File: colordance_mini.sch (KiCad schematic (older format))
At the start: 36 parts, among them J1 CONN_02X08, J2 CONN_02X08, SW1 Rotary_Encoder, SW2 Rotary_Encoder, SW3 Rotary_Encoder, SW4 Rotary_Encoder

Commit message: Create the PCB. This is rev v1.0, I requested 5 boards from EasyEDA. As-yet untested.
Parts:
- removed J2: CONN_02X08, symbol CONN_02X08
- added C10: 10uF, Capacitors_THT:CP_Radial_D5.0mm_P2.00mm, symbol CP
- added C9: .01uF, Capacitors_THT:C_Disc_D5.0mm_W2.5mm_P5.00mm, symbol C
- C1, C2, C3, C4, C5, C6, C7, C8: footprint (none) -> Capacitors_THT:C_Disc_D5.0mm_W2.5mm_P5.00mm
- J1: footprint (none) -> Pin_Headers:Pin_Header_Straight_2x08_Pitch2.54mm
- R1, R10, R11, R12, R13, R14, R15, R16, R2, R3, R4, R5, R6, R7, R8, R9: footprint (none) -> Resistors_THT:R_Axial_DIN0207_L6.3mm_D2.5mm_P7.62mm_Horizontal
- RV1, RV2, RV3, RV4, RV5, RV6: footprint (none) -> homebrew:BOURNS_SLIDE_POT
- SW1, SW2, SW3, SW4: footprint (none) -> homebrew:BOURNS_PEC11R_ENCODER
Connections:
- net labels added: SAT, VAL
- net labels removed: SATURATION, VALUE
- wire segments 112 -> 98
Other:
- moved on the sheet: RV2, RV3, RV4, RV5, RV6

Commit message: Add front panel SVG v1.0
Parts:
- RV1, RV2, RV3, RV4, RV5, RV6: footprint homebrew:BOURNS_SLIDE_POT -> homebrew:BOURNS_SLIDE_POT_45MM
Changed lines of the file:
@@
 LIBS:contrib
 LIBS:valves
+LIBS:colordance_mini-cache
 EELAYER 25 0
 EELAYER END
@@
 F 0 "RV1" V 625 2300 50  0000 C CNN
 F 1 "POT" V 700 2300 50  0000 C CNN
-F 2 "homebrew:BOURNS_SLIDE_POT" H 800 2300 50  0001 C CNN
+F 2 "homebrew:BOURNS_SLIDE_POT_45MM" H 800 2300 50  0001 C CNN
 F 3 "" H 800 2300 50  0001 C CNN
 	1    800  2300
@@
 F 0 "RV2" V 1325 2300 50  0000 C CNN
 F 1 "POT" V 1400 2300 50  0000 C CNN
-F 2 "homebrew:BOURNS_SLIDE_POT" H 1500 2300 50  0001 C CNN
+F 2 "homebrew:BOURNS_SLIDE_POT_45MM" H 1500 2300 50  0001 C CNN
 F 3 "" H 1500 2300 50  0001 C CNN
 	1    1500 2300
@@
 F 0 "RV3" V 2025 2300 50  0000 C CNN
 F 1 "POT" V 2100 2300 50  0000 C CNN
-F 2 "homebrew:BOURNS_SLIDE_POT" H 2200 2300 50  0001 C CNN
+F 2 "homebrew:BOURNS_SLIDE_POT_45MM" H 2200 2300 50  0001 C CNN
 F 3 "" H 2200 2300 50  0001 C CNN
 	1    2200 2300
@@
 F 0 "RV4" V 2875 2300 50  0000 C CNN
 F 1 "POT" V 2950 2300 50  0000 C CNN
-F 2 "homebrew:BOURNS_SLIDE_POT" H 3050 2300 50  0001 C CNN
+F 2 "homebrew:BOURNS_SLIDE_POT_45MM" H 3050 2300 50  0001 C CNN
 F 3 "" H 3050 2300 50  0001 C CNN
 	1    3050 2300
@@
 F 0 "RV5" V 3575 2300 50  0000 C CNN
 F 1 "POT" V 3650 2300 50  0000 C CNN
-F 2 "homebrew:BOURNS_SLIDE_POT" H 3750 2300 50  0001 C CNN
+F 2 "homebrew:BOURNS_SLIDE_POT_45MM" H 3750 2300 50  0001 C CNN
 F 3 "" H 3750 2300 50  0001 C CNN
 	1    3750 2300
@@
 F 0 "RV6" V 4375 2300 50  0000 C CNN
 F 1 "POT" V 4450 2300 50  0000 C CNN
-F 2 "homebrew:BOURNS_SLIDE_POT" H 4550 2300 50  0001 C CNN
+F 2 "homebrew:BOURNS_SLIDE_POT_45MM" H 4550 2300 50  0001 C CNN
 F 3 "" H 4550 2300 50  0001 C CNN
 	1    4550 2300

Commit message: Add a teensy and a whole bunch of actuators for v1.1.
Layout not yet updated.
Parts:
- removed C10: 10uF, Capacitors_THT:CP_Radial_D5.0mm_P2.00mm, symbol CP
- removed J1: CONN_02X08, Pin_Headers:Pin_Header_Straight_2x08_Pitch2.54mm, symbol CONN_02X08
- added C12, C8: 10uF, Capacitors_THT:C_Disc_D5.0mm_W2.5mm_P5.00mm, symbol C
- added C7: .01uF, Capacitors_THT:C_Disc_D5.0mm_W2.5mm_P5.00mm, symbol C
- added J1: XLR3, symbol XLR3
- added J10: CONN_01X06, symbol CONN_01X06
- added J11, J12, J17, J3, J5, J7, J8, J9: CONN_01X04, symbol CONN_01X04
- added J13, J14, J15, J16, J4, J6: CONN_01X03, symbol CONN_01X03
- added J2: CONN_01X08, symbol CONN_01X08
- added R1: 120, symbol R
- added R2: 3k3, symbol R
- added R22: 470, symbol R
- added R23, R24, R25: 4k7, symbol R
- added R3: 1k, symbol R
- added R4, R5: 562, symbol R
- added U1: MAX485CSA+, 21-0041B_8, symbol MAX485CSA+
- added U2: ROE-0505S, symbol ROE-0505S
- added U3: 6N137, DIP762W50P254L977H451Q8, symbol 6N137
- added U4: Teensy3.5, symbol Teensy3.5-RESCUE-colordance_mini
- renumbered C8 to C10, C9 to C11, C7 to C9, R5 to R10, R6 to R11, R7 to R12, R8 to R13, R9 to R14, R10 to R15, R11 to R16, R12 to R17, R13 to R18, R14 to R19, R15 to R20, R16 to R21, R1 to R6, R2 to R7, R3 to R8, R4 to R9, RV3 to RV2, RV4 to RV3, RV5 to RV4, RV6 to RV5, RV2 to RV6
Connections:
- net labels added: +3V3, +5V, +BATT, AUX_CS, AUX_MISO, AUX_MOSI, AUX_PIN_1, AUX_PIN_2, AUX_RX, AUX_SCK, AUX_TX, DENSITY, DMX_3V3, DMX_3V3_ISO, HUE_0_A, HUE_0_B, HUE_1_A, HUE_1_B, HUE_2_A, HUE_2_B, MIC_IN, MOTION_1, MOTION_2, MOTION_3, MOTION_4, NEXT_EFFECT, NEXT_EFFECT_LED, ON_BUTTON, ON_BUTTON_LED, ORIENTATION, ORIENTATION_LED, PARAM, PREV_EFFECT, PREV_EFFECT_LED, SCL0, SDA0, SERIAL_LOG_OUT, SPI_LED_MOSI, SPI_LED_SCK, TEMPO_A, TEMPO_B, TEMPO_TAP, TEMPO_TAP_LED, VBATT_DIV, VDMX
- net labels removed: E1_A, E1_B, E2_A, E2_B, E3_A, E3_B, HUE_A, HUE_B, SAT, VAL, VCC
- wire segments 98 -> 101
- no-connect marks 0 -> 37
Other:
- note added: "Aux connections"
- note added: "Aux pins"
- note added: "Battery voltage monitor"
- note added: "Buttons"
- note added: "DMX"
- note added: "DMX power isolation"
- note added: "DMX signal isolation"
- note added: "External mic"
- note added: "I2C"
- note added: "Logger"
- note added: "Motion sensors"
- note added: "On button"
- note added: "Orientation"
- note added: "Power"
- note added: "Prev/next effect"
- note added: "SPI"
- note added: "SPI LED connections"
- note added: "Serial"
- note added: "Tempo"
- moved on the sheet: C11, RV2, RV3, RV4, RV5, RV6

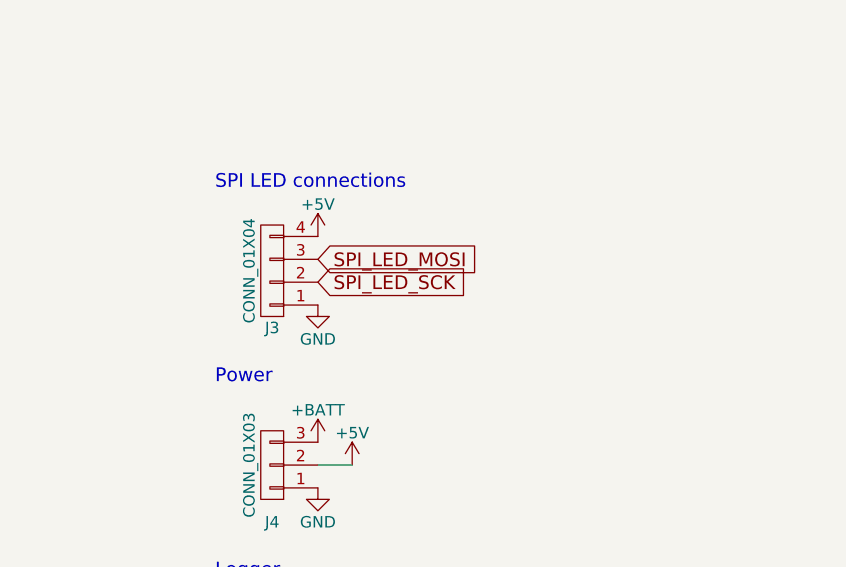
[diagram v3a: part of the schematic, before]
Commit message: Add an onboard APA102 LED
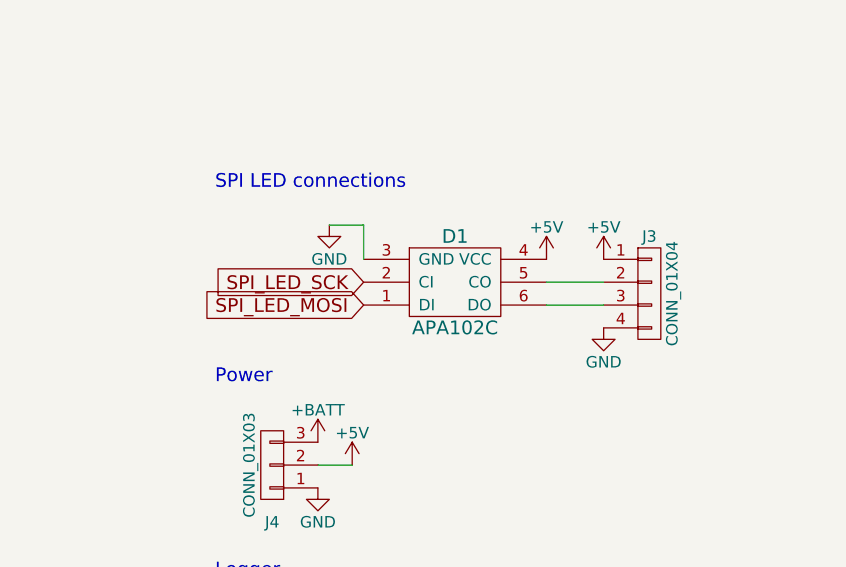
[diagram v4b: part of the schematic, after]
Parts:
- added D1: APA102C, symbol APA102C
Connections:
- net +5V: now also J3.1 (P1), D1.4 (VCC); no longer J3.4 (P4)
- net GND: now also J3.4 (P4), D1.3 (GND); no longer J3.1 (P1)
- net SPI_LED_MOSI: now also D1.1 (DI); no longer J3.3 (P3)
- net SPI_LED_SCK: now also D1.2 (CI); no longer J3.2 (P2)
- new net: D1.5 (CO), J3.2 (P2)
- new net: D1.6 (DO), J3.3 (P3)
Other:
- moved on the sheet: J3
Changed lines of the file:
@@
 L CONN_01X04 J3
 U 1 1 5ABFCD70
-P 12250 5550
-F 0 "J3" H 12250 5800 50  0000 C CNN
-F 1 "CONN_01X04" V 12350 5550 50  0000 C CNN
-F 2 "" H 12250 5550 50  0001 C CNN
-F 3 "" H 12250 5550 50  0001 C CNN
-	1    12250 5550
-	-1   0    0    1
+P 13900 5650
+F 0 "J3" H 13900 5900 50  0000 C CNN
+F 1 "CONN_01X04" V 14000 5650 50  0000 C CNN
+F 2 "" H 13900 5650 50  0001 C CNN
+F 3 "" H 13900 5650 50  0001 C CNN
+	1    13900 5650
+	1    0    0    -1
 $EndComp
 Text Notes 12000 5200 0    60   ~ 0
 SPI LED connections
-Text GLabel 12450 5500 2    60   Input ~ 0
+Text GLabel 12650 5700 0    60   Input ~ 0
 SPI_LED_MOSI
-Text GLabel 12450 5600 2    60   Input ~ 0
+Text GLabel 12650 5600 0    60   Input ~ 0
 SPI_LED_SCK
 $Comp
 L +5V #PWR039
 U 1 1 5ABFD543
-P 12450 5400
-F 0 "#PWR039" H 12450 5250 50  0001 C CNN
-F 1 "+5V" H 12450 5540 50  0000 C CNN
-F 2 "" H 12450 5400 50  0001 C CNN
-F 3 "" H 12450 5400 50  0001 C CNN
-	1    12450 5400
+P 13700 5500
+F 0 "#PWR039" H 13700 5350 50  0001 C CNN
+F 1 "+5V" H 13700 5640 50  0000 C CNN
+F 2 "" H 13700 5500 50  0001 C CNN
+F 3 "" H 13700 5500 50  0001 C CNN
+	1    13700 5500
 	1    0    0    -1
 $EndComp
@@
 L GND #PWR040
 U 1 1 5ABFD6A5
-P 12450 5700
-F 0 "#PWR040" H 12450 5450 50  0001 C CNN
-F 1 "GND" H 12450 5550 50  0000 C CNN
-F 2 "" H 12450 5700 50  0001 C CNN
-F 3 "" H 12450 5700 50  0001 C CNN
-	1    12450 5700
+P 13700 5800
+F 0 "#PWR040" H 13700 5550 50  0001 C CNN
+F 1 "GND" H 13700 5650 50  0000 C CNN
+F 2 "" H 13700 5800 50  0001 C CNN
+F 3 "" H 13700 5800 50  0001 C CNN
+	1    13700 5800
 	1    0    0    -1
 $EndComp
@@
 NoConn ~ 19050 4000
 Connection ~ 1250 9150
+$Comp
+L APA102C D1
+U 1 1 5AC13E31
+P 13050 5600
+F 0 "D1" H 13050 5800 60  0000 C CNN
+F 1 "APA102C" H 13050 5400 60  0000 C CNN
+F 2 "" H 13050 5600 60  0001 C CNN
+F 3 "" H 13050 5600 60  0001 C CNN
+	1    13050 5600
+	1    0    0    -1
+$EndComp
+$Comp
+L GND #PWR072
+U 1 1 5AC140CF
+P 12500 5350
+F 0 "#PWR072" H 12500 5100 50  0001 C CNN
+F 1 "GND" H 12500 5200 50  0000 C CNN
+F 2 "" H 12500 5350 50  0001 C CNN
+F 3 "" H 12500 5350 50  0001 C CNN
+	1    12500 5350
+	1    0    0    -1
+$EndComp
+Wire Wire Line
+	12500 5350 12650 5350
+Wire Wire Line
+	12650 5350 12650 5500
+$Comp
+L +5V #PWR073
+U 1 1 5AC14273
+P 13450 5500
+F 0 "#PWR073" H 13450 5350 50  0001 C CNN
+F 1 "+5V" H 13450 5640 50  0000 C CNN
+F 2 "" H 13450 5500 50  0001 C CNN
+F 3 "" H 13450 5500 50  0001 C CNN
+	1    13450 5500
+	1    0    0    -1
+$EndComp
+Wire Wire Line
+	13450 5600 13700 5600
+Wire Wire Line
+	13700 5700 13450 5700
 $EndSCHEMATC

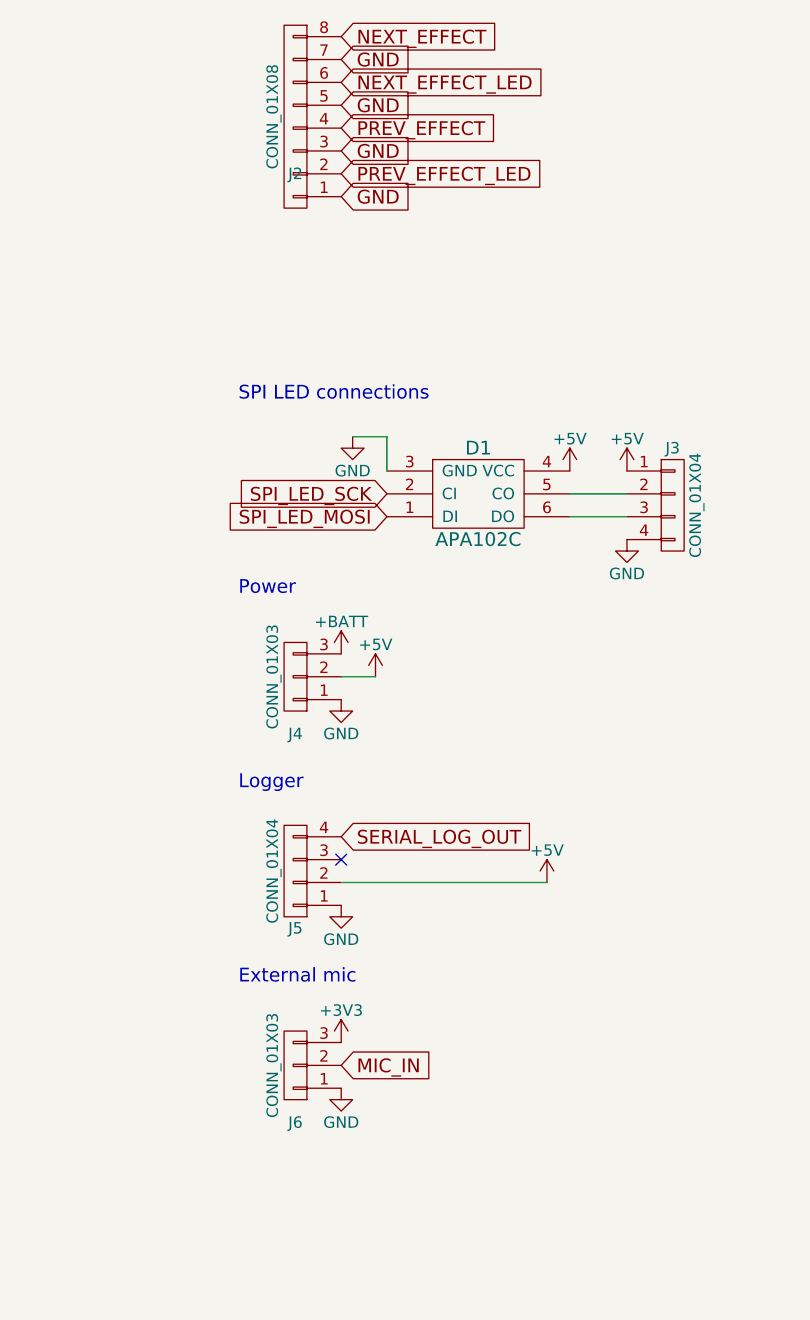
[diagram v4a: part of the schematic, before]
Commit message: Rough placement
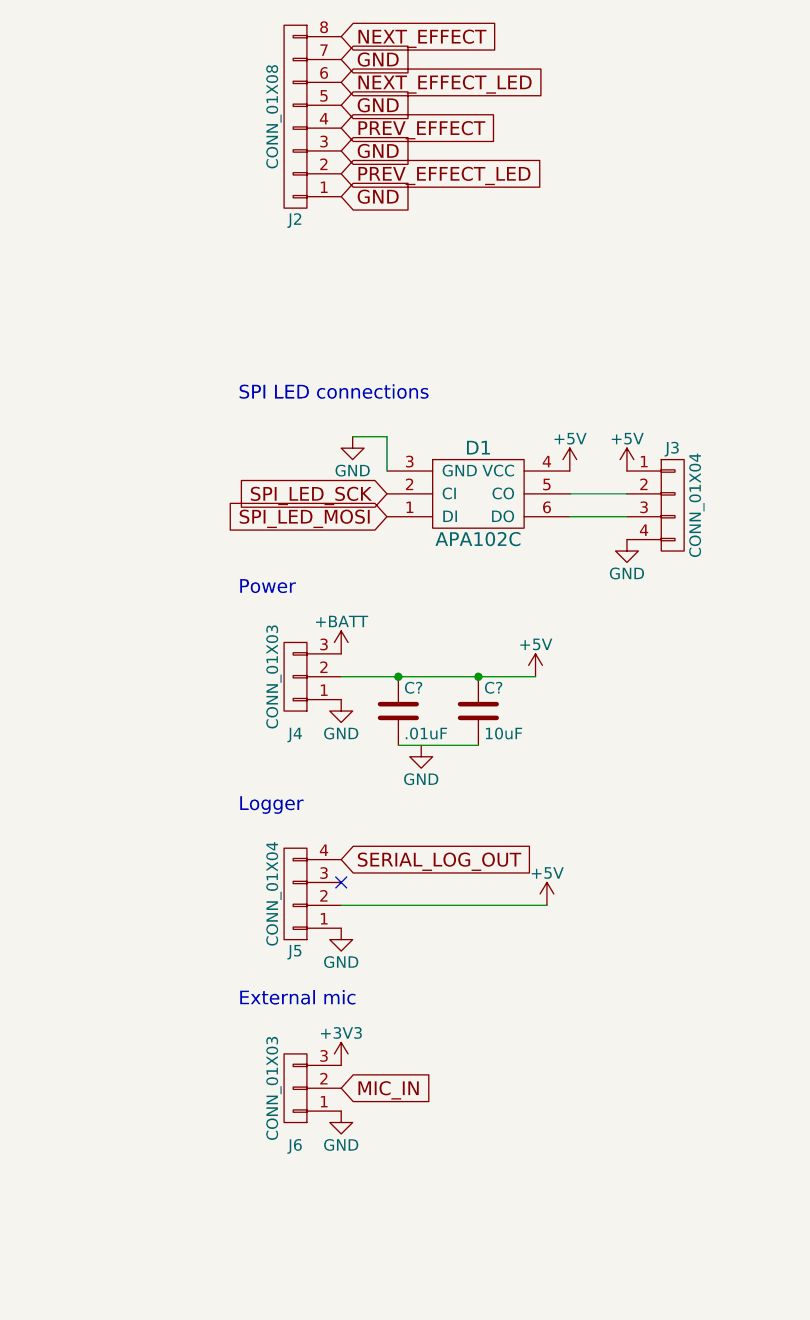
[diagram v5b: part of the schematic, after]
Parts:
- added C?: .01uF, Capacitors_SMD:C_0603_HandSoldering, symbol C
- added C?: 10uF, Capacitors_SMD:C_0603_HandSoldering, symbol C
- C1, C10, C11, C12, C2, C3, C4, C5, C6, C7, C8, C9: footprint Capacitors_THT:C_Disc_D5.0mm_W2.5mm_P5.00mm -> Capacitors_SMD:C_0603_HandSoldering
- D1: footprint (none) -> Sparkfun-LED:APA102C
- J1: footprint (none) -> shardy:XLR-NC3FA
- J10: footprint (none) -> Pin_Headers:Pin_Header_Straight_1x06_Pitch2.54mm
- J11, J12, J17, J5: footprint (none) -> Pin_Headers:Pin_Header_Straight_1x04_Pitch2.54mm
- J13, J14, J15, J16, J6: footprint (none) -> Pin_Headers:Pin_Header_Straight_1x03_Pitch2.54mm
- J2: footprint (none) -> homebrew:1985250_phoenix_8pos_3.5mm
- J3, J4, J7, J8, J9: footprint (none) -> homebrew:1985218_phoenix_4pos_3.5mm
- R1, R2, R22, R23, R24, R25, R3, R4, R5: footprint (none) -> Resistors_SMD:R_0603_HandSoldering
- R10, R11, R12, R13, R14, R15, R16, R17, R18, R19, R20, R21, R6, R7, R8, R9: footprint Resistors_THT:R_Axial_DIN0207_L6.3mm_D2.5mm_P7.62mm_Horizontal -> Resistors_SMD:R_0603_HandSoldering
- U1: footprint 21-0041B_8 -> SMD_Packages:SOIC-8-N
- U2: footprint (none) -> arduino-micro-dmx:ROE-0505S
- U3: footprint DIP762W50P254L977H451Q8 -> 6N137:DIP762W50P254L977H451Q8
- U4: footprint (none) -> teensy:Teensy35_36
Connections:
- net +5V: now also C?.1, C?.1
- new net: C?.2, C?.2
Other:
- moved on the sheet: J5, J6

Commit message: Placement finished
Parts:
- J1: footprint shardy:XLR-NC3FA -> homebrew:NC3FAH
- gave numbers to parts that had none: 2
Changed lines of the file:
@@
 F 0 "J1" H 1400 9000 50  0000 C CNN
 F 1 "XLR3" H 1450 8500 50  0000 C CNN
-F 2 "shardy:XLR-NC3FA" H 1250 8750 50  0001 C CNN
+F 2 "homebrew:NC3FAH" H 1250 8750 50  0001 C CNN
 F 3 "" H 1250 8750 50  0001 C CNN
 	1    1250 8750
@@
 	13700 5700 13450 5700
 $Comp
-L C C?
+L C C13
 U 1 1 5AC21BC3
 P 12700 6550
-F 0 "C?" H 12725 6650 50  0000 L CNN
+F 0 "C13" H 12725 6650 50  0000 L CNN
 F 1 ".01uF" H 12725 6450 50  0000 L CNN
 F 2 "Capacitors_SMD:C_0603_HandSoldering" H 12738 6400 50  0001 C CNN
@@
 $EndComp
 $Comp
-L C C?
+L C C14
 U 1 1 5AC21CFD
 P 13050 6550
-F 0 "C?" H 13075 6650 50  0000 L CNN
+F 0 "C14" H 13075 6650 50  0000 L CNN
 F 1 "10uF" H 13075 6450 50  0000 L CNN
 F 2 "Capacitors_SMD:C_0603_HandSoldering" H 13088 6400 50  0001 C CNN
@@
 	13050 6700 12700 6700
 $Comp
-L GND #PWR?
+L GND #PWR074
 U 1 1 5AC22B68
 P 12800 6700
-F 0 "#PWR?" H 12800 6450 50  0001 C CNN
+F 0 "#PWR074" H 12800 6450 50  0001 C CNN
 F 1 "GND" H 12800 6550 50  0000 C CNN
 F 2 "" H 12800 6700 50  0001 C CNN

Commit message: Routing finished
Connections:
- net +3V3: now also J5.2 (P2)
- net +5V: no longer J5.2 (P2)
- net GND: now also C13.2, C14.2
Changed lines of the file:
@@
 Logger
-$Comp
-L +5V #PWR052
-U 1 1 5AC053EA
-P 13350 7400
-F 0 "#PWR052" H 13350 7250 50  0001 C CNN
-F 1 "+5V" H 13350 7540 50  0000 C CNN
-F 2 "" H 13350 7400 50  0001 C CNN
-F 3 "" H 13350 7400 50  0001 C CNN
-	1    13350 7400
-	1    0    0    -1
-$EndComp
 $Comp
 L GND #PWR053
@@
 	1    0    0    -1
 $EndComp
+Connection ~ 7050 5200
+Connection ~ 12800 6700
+$Comp
+L +3V3 #PWR?
+U 1 1 5AC2FC7B
+P 13350 7400
+F 0 "#PWR?" H 13350 7250 50  0001 C CNN
+F 1 "+3V3" H 13350 7540 50  0000 C CNN
+F 2 "" H 13350 7400 50  0001 C CNN
+F 3 "" H 13350 7400 50  0001 C CNN
+	1    13350 7400
+	1    0    0    -1
+$EndComp
